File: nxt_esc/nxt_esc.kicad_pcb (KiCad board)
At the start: 2 copper layers, 46.4 x 55.2 mm, 15 parts, among them IC1 L293D, J1 NXT_MOTOR, J2 NXT_MOTOR, SW1 Skid Steer/Drive & Steer, U1 LM7809CT

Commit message: Updated PCB
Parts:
- added C4: 100u, Capacitors_ThroughHole:CP_Radial_D5.0mm_P2.50mm, F.Cu at (154.3, 55.9)
- added C5: 0.1 u, Capacitors_ThroughHole:C_Disc_D3.4mm_W2.1mm_P2.50mm, F.Cu at (158.8, 59.1)
- added C6: 100u, Capacitors_ThroughHole:CP_Radial_D5.0mm_P2.50mm, F.Cu at (153.0, 99.1)
- added C7: 100u, Capacitors_ThroughHole:CP_Radial_D5.0mm_P2.50mm, F.Cu at (160.7, 99.1)
- added C8: 0.1 u, Capacitors_ThroughHole:C_Disc_D3.4mm_W2.1mm_P2.50mm, F.Cu at (159.4, 106.0)
- added C9: 0.1 u, Capacitors_ThroughHole:C_Disc_D3.4mm_W2.1mm_P2.50mm, F.Cu at (153.7, 106.0)
- C3: value 0.1u -> 0.1 u
- U1: value LM7809CT -> LM7805CT
- moved J1 4.44 mm to (171.4, 97.8)
- moved J2 3.81 mm to (141.6, 97.8)
- moved RC1 3.17 mm to (171.4, 57.8)
- moved C2 2.13 mm to (150.0, 88.3), turned to 180 degrees
- moved BT1 1.27 mm to (144.8, 58.4)
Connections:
- BT1 pad 1: Net-(BT1-Pad1) -> VCC
- C3 pad 1: Net-(C2-Pad1) -> GND
- C3 pad 2: GND -> Net-(C2-Pad1)
- U1 pad 1: Net-(BT1-Pad1) -> VCC
- U1 pad 3: VCC -> Net-(C2-Pad1)
- uP1 pad 19: VCC -> Net-(C2-Pad1)
- uP1 pad 22: Net-(C2-Pad1) -> Net-(uP1-Pad22)
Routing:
- net Net-(C2-Pad1): track 121.9 -> 163.5 mm
- net VCC: track 39.9 -> 20.4 mm
- net GND: track 140.1 -> 154.5 mm
- net Net-(C7-Pad2): track 0.00 -> 10.9 mm
- net Net-(C6-Pad2): track 0.00 -> 10.7 mm
- net Net-(IC1-Pad1): track 21.0 -> 31.0 mm
- net Net-(BT1-Pad1): track 9.68 -> 0.00 mm
- net Net-(IC1-Pad15): track 45.6 -> 39.7 mm
- net Net-(J1-Pad6): track 22.3 -> 26.8 mm
- net Net-(J1-Pad5): track 29.3 -> 33.7 mm
- net Net-(IC1-Pad2): track 12.8 -> 16.9 mm
- net Net-(J2-Pad5): track 32.6 -> 36.6 mm
- net Net-(IC1-Pad3): track 40.0 -> 36.3 mm
- net Net-(IC1-Pad14): track 22.0 -> 18.5 mm
- net Net-(IC1-Pad10): track 46.2 -> 49.2 mm
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
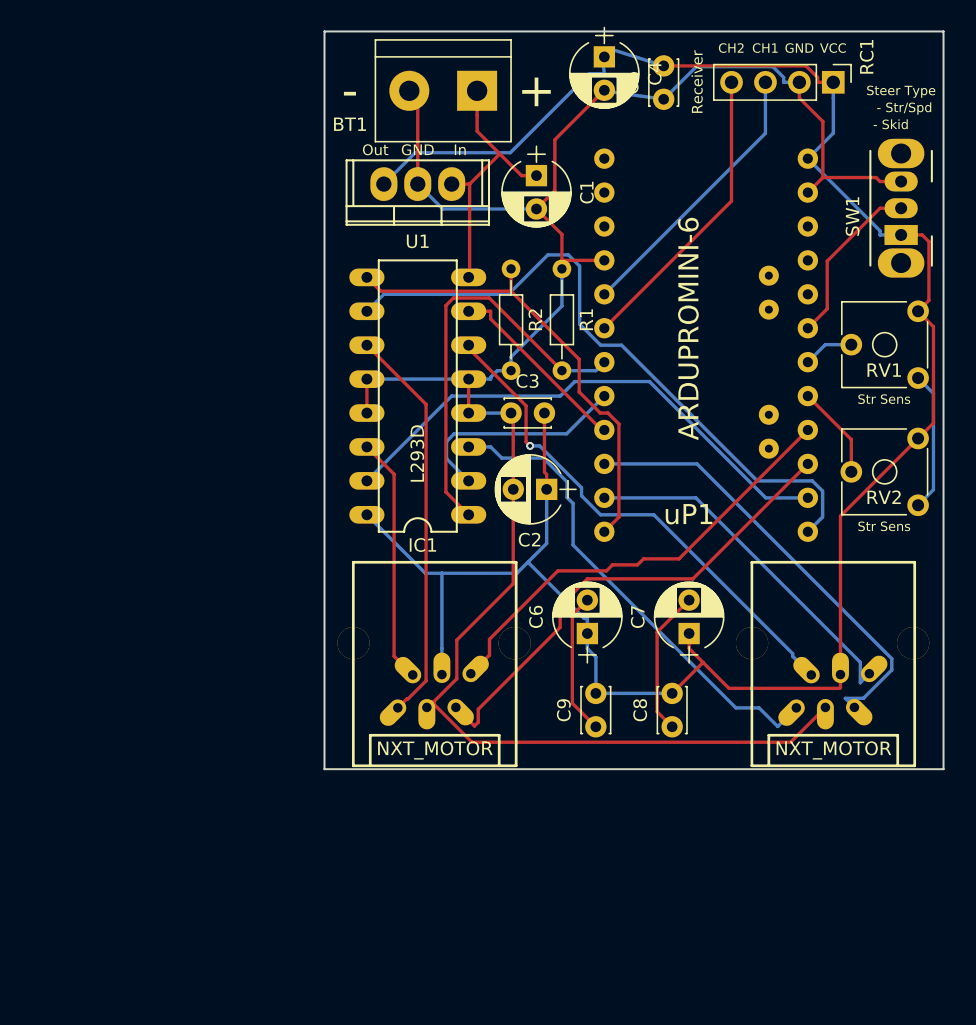
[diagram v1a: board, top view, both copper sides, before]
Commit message: Resized board to 6x6 Lego size
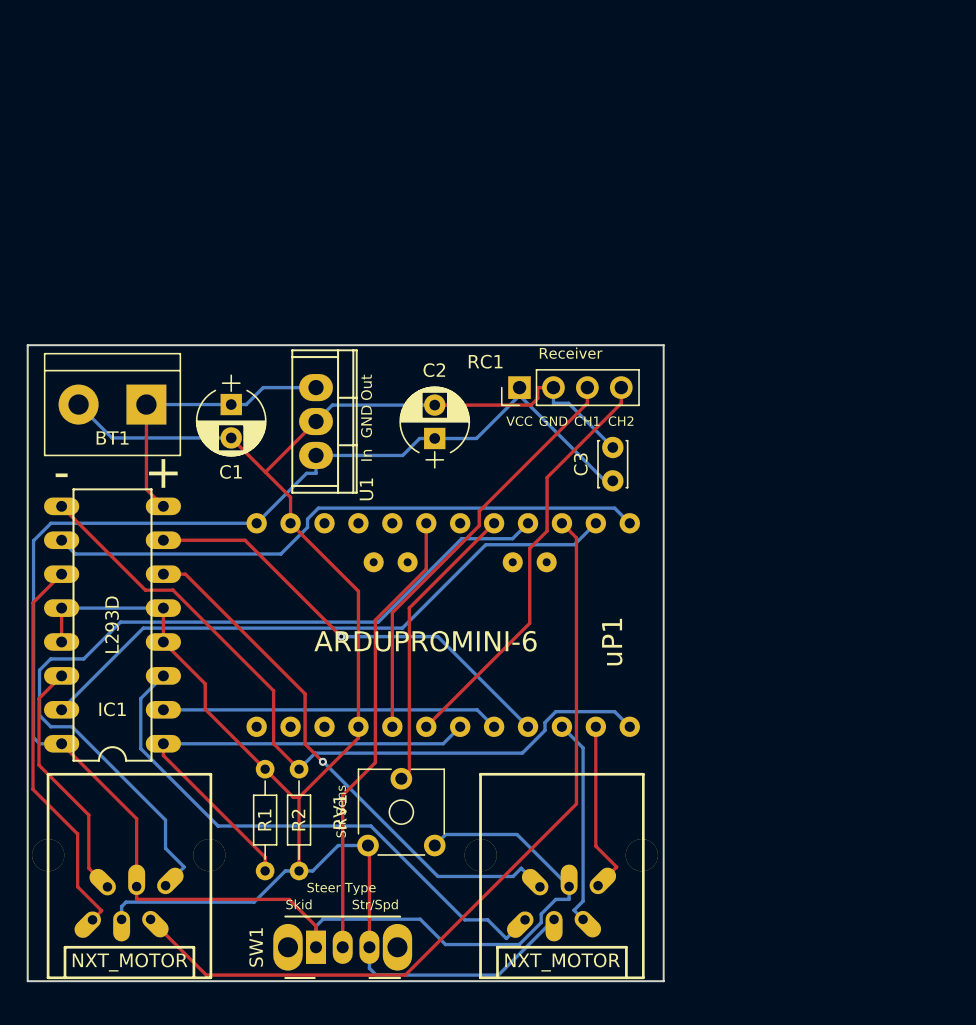
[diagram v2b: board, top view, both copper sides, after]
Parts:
- removed C4, C6, C7: 100u, Capacitors_ThroughHole:CP_Radial_D5.0mm_P2.50mm
- removed C5, C8, C9: 0.1 u, Capacitors_ThroughHole:C_Disc_D3.4mm_W2.1mm_P2.50mm
- removed RV2: Steering Sensitivity, Potentiometers:Potentiometer_Trimmer_ACP_CA6v_Horizontal
- RV1: value Steering Trim -> Steering Sensitivity
- moved SW1 69.0 mm to (132.7, 122.6), turned to 0 degrees
- moved uP1 59.5 mm to (121.9, 108.6), turned to 90 degrees
- moved RV1 53.9 mm to (141.6, 114.9), turned to 90 degrees
- moved R1 43.6 mm to (128.9, 109.2)
- moved R2 40.7 mm to (131.4, 109.2)
- moved BT1 34.1 mm to (120.0, 81.9)
- moved RC1 32.8 mm to (148.0, 80.6), turned to 90 degrees
- moved IC1 28.6 mm to (117.5, 98.4)
- moved C1 28.6 mm to (126.4, 81.9)
- moved J2 27.8 mm to (118.7, 113.7)
- moved J1 25.8 mm to (151.1, 113.7)
- moved U1 19.3 mm to (132.7, 83.2), turned to 270 degrees
- moved C2 9.21 mm to (141.6, 84.5), turned to 90 degrees
- moved C3 9.16 mm to (154.9, 87.6), turned to 90 degrees
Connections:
- C3 pad 1: GND -> Net-(C2-Pad1)
- C3 pad 2: Net-(C2-Pad1) -> GND
- RV1 pad 3: Net-(RV1-Pad3) -> GND
- uP1 pad 25: Net-(RV1-Pad2) -> Net-(uP1-Pad25)
- uP1 pad 26: Net-(RV2-Pad2) -> Net-(RV1-Pad2)
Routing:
- net Net-(J2-Pad6): track 33.5 -> 63.3 mm
- net Net-(C2-Pad1): track 163.5 -> 135.0 mm
- net Net-(J2-Pad5): track 36.6 -> 60.4 mm
- net Net-(SW1-Pad2): track 12.8 -> 34.3 mm
- net Net-(IC1-Pad9): track 35.0 -> 55.6 mm
- net Net-(IC1-Pad7): track 14.2 -> 33.1 mm, vias 0 -> 1
- net Net-(RV1-Pad2): track 3.80 -> 22.0 mm
- net Net-(J1-Pad5): track 33.7 -> 15.6 mm
- net Net-(J1-Pad6): track 26.8 -> 13.1 mm
- net Net-(C7-Pad2): track 10.9 -> 0.00 mm
- net Net-(C6-Pad2): track 10.7 -> 0.00 mm
- net Net-(RC1-Pad3): track 20.9 -> 31.4 mm
- net Net-(RV1-Pad3): track 10.5 -> 0.00 mm
- net Net-(RC1-Pad4): track 22.4 -> 31.4 mm
- net Net-(IC1-Pad2): track 16.9 -> 25.3 mm
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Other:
- board size 46.4 x 55.2 mm -> 47.6 x 47.6 mm
- board text added: "Skid"
- board text added: "Str/Spd"
- board text removed: "- Skid"
- board text removed: "- Str/Spd"

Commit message: Added center steering button
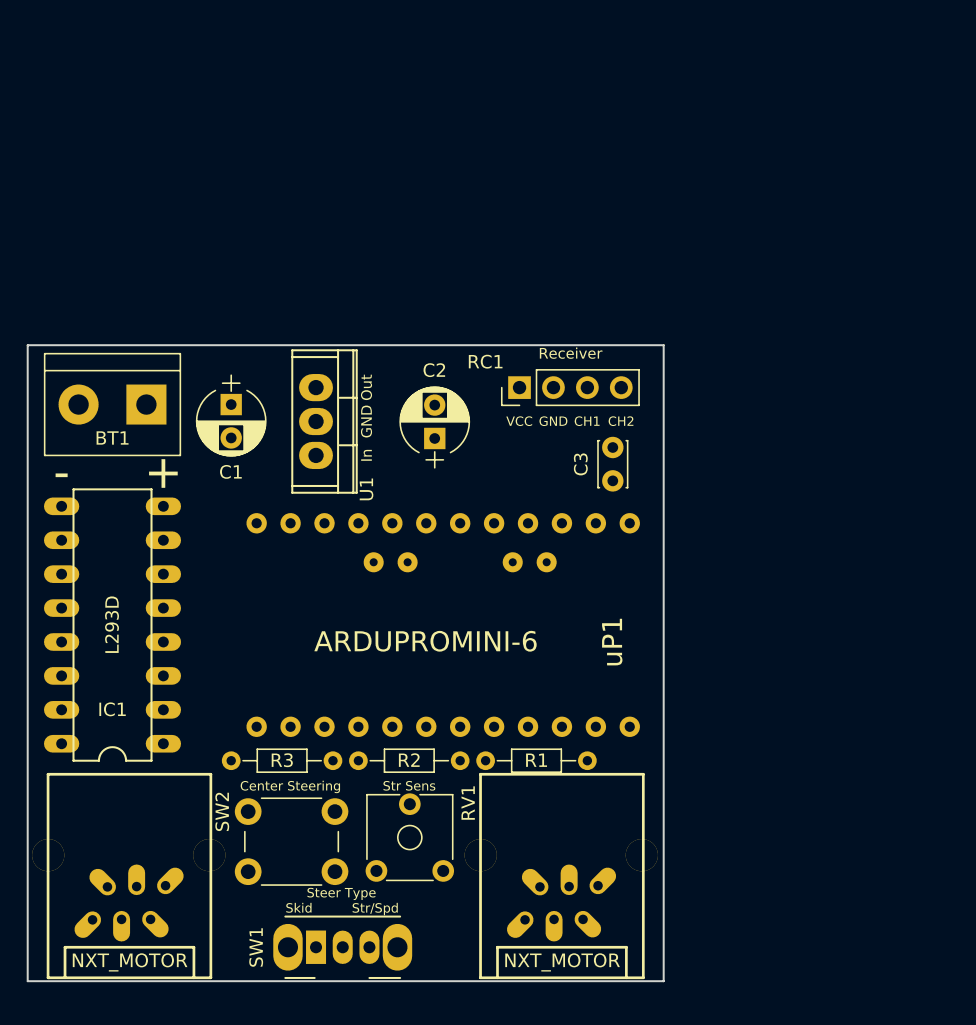
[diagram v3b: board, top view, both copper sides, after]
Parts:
- added R3: 100k, Resistors_ThroughHole:R_Axial_DIN0204_L3.6mm_D1.6mm_P7.62mm_Horizontal, F.Cu at (126.4, 108.6)
- added SW2: Center Steering, Buttons_Switches_ThroughHole:SW_PUSH_6mm, F.Cu at (127.6, 112.4)
- moved R1 16.5 mm to (145.4, 108.6), turned to 0 degrees
- moved R2 12.1 mm to (143.5, 108.6), turned to 180 degrees
- moved RV1 2.01 mm to (142.2, 116.8)
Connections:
- uP1 pad 21: Net-(uP1-Pad21) -> (no net)
- uP1 pad 22: Net-(uP1-Pad22) -> (no net)
- uP1 pad 23: Net-(uP1-Pad23) -> (no net)
- uP1 pad 31: Net-(uP1-Pad31) -> (no net)
- uP1 pad 32: Net-(uP1-Pad32) -> (no net)
- uP1 pad 34: Net-(uP1-Pad34) -> (no net)
- uP1 pad 35: Net-(uP1-Pad35) -> (no net)
- uP1 pad 7: Net-(uP1-Pad7) -> (no net)
- uP1 pad 8: Net-(uP1-Pad8) -> (no net)
- uP1 pad 9: Net-(uP1-Pad9) -> (no net)
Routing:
- net GND: track 157.4 -> 0.00 mm
- net Net-(C2-Pad1): track 135.0 -> 0.00 mm
- net Net-(J2-Pad6): track 63.3 -> 0.00 mm
- net Net-(J2-Pad5): track 60.4 -> 0.00 mm
- net Net-(IC1-Pad9): track 55.6 -> 0.00 mm
- net Net-(IC1-Pad15): track 45.8 -> 0.00 mm
- net Net-(IC1-Pad10): track 45.2 -> 0.00 mm
- net Net-(IC1-Pad3): track 41.4 -> 0.00 mm
- net Net-(IC1-Pad6): track 40.6 -> 0.00 mm, vias 1 -> 0
- net Net-(IC1-Pad1): track 35.4 -> 0.00 mm
- net Net-(SW1-Pad2): track 34.3 -> 0.00 mm
- net Net-(IC1-Pad7): track 33.1 -> 0.00 mm, vias 1 -> 0
- net Net-(RC1-Pad4): track 31.4 -> 0.00 mm
- net Net-(RC1-Pad3): track 31.4 -> 0.00 mm
- net Net-(IC1-Pad11): track 29.2 -> 0.00 mm
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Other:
- board text added: "Center Steering"

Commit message: Added motor jack labels. Forgot to route wires.
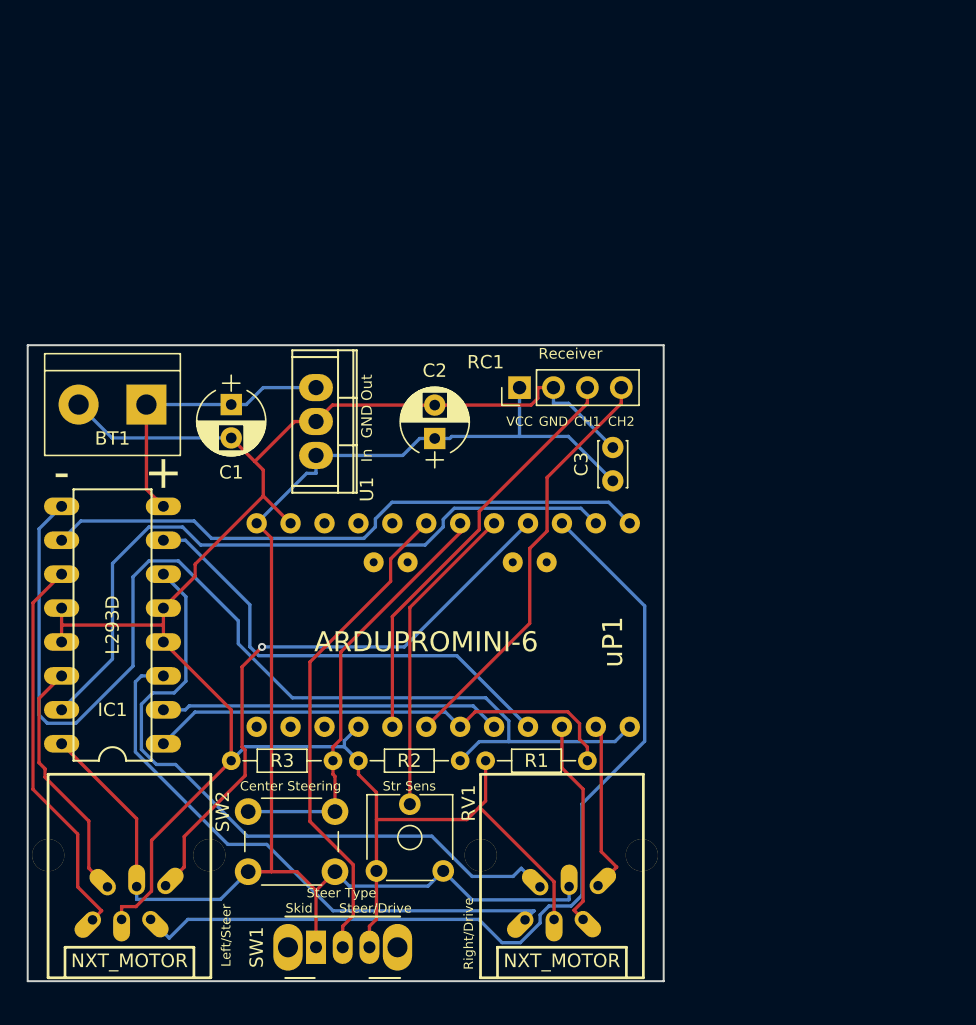
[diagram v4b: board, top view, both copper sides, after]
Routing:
- net GND: track 0.00 -> 153.5 mm
- net Net-(C2-Pad1): track 0.00 -> 117.2 mm
- net Net-(IC1-Pad9): track 0.00 -> 82.0 mm
- net Net-(J2-Pad5): track 0.00 -> 68.4 mm
- net Net-(IC1-Pad15): track 0.00 -> 52.4 mm
- net Net-(IC1-Pad6): track 0.00 -> 50.8 mm
- net Net-(IC1-Pad10): track 0.00 -> 45.8 mm
- net Net-(J2-Pad6): track 0.00 -> 44.8 mm, vias 0 -> 1
- net Net-(IC1-Pad3): track 0.00 -> 43.3 mm
- net Net-(SW1-Pad2): track 0.00 -> 37.0 mm
- net Net-(IC1-Pad1): track 0.00 -> 36.5 mm
- net Net-(IC1-Pad7): track 0.00 -> 34.9 mm
- net Net-(R3-Pad2): track 0.00 -> 32.1 mm
- net Net-(RC1-Pad4): track 0.00 -> 31.4 mm
- net Net-(RC1-Pad3): track 0.00 -> 31.4 mm
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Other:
- board text added: "Left/Steer"
- board text added: "Right/Drive"
- board text added: "Steer/Drive"
- board text removed: "Str/Spd"

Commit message: Added reverse polarity protection diode and power switch
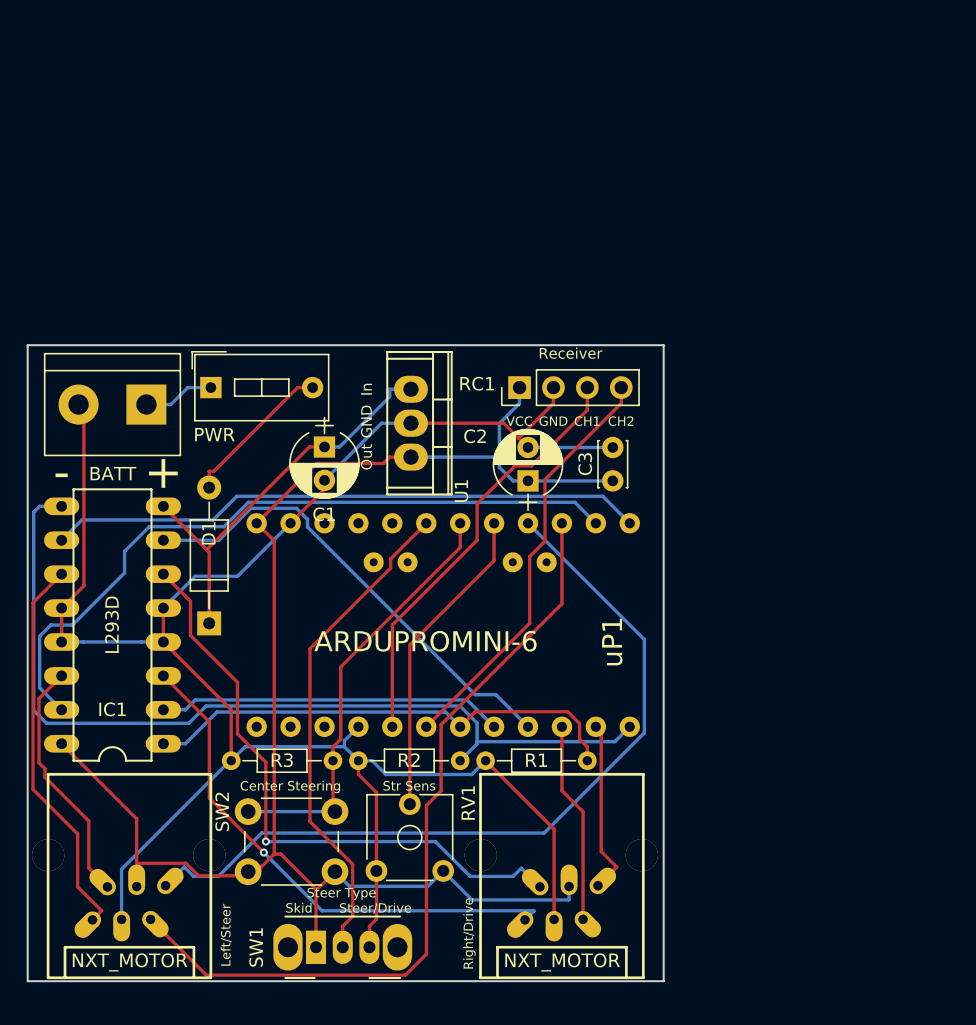
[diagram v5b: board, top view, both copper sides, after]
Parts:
- added D1: D_Schottky, Diodes_ThroughHole:D_A-405_P10.16mm_Horizontal, F.Cu at (124.7, 98.3)
- added PWR: SPST, Buttons_Switches_ThroughHole:SW_DIP_x1_W7.62mm_Slide, F.Cu at (124.8, 80.6)
- moved C2 7.67 mm to (148.6, 87.6)
- moved C1 7.67 mm to (133.3, 85.1)
- moved U1 7.11 mm to (139.8, 83.3)
- renumbered BT1 to BATT
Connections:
- BATT pad 1: VCC -> Net-(BT1-Pad1)
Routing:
- net Net-(J2-Pad6): track 44.8 -> 60.5 mm, vias 1 -> 0
- net Net-(IC1-Pad9): track 82.0 -> 67.0 mm
- net Net-(D1-Pad2): track 0.00 -> 11.6 mm
- net VCC: track 21.4 -> 30.8 mm
- net Net-(J2-Pad5): track 68.4 -> 59.5 mm
- net Net-(BT1-Pad1): track 0.00 -> 5.35 mm
- net Net-(IC1-Pad6): track 50.8 -> 45.6 mm, vias 0 -> 1
- net Net-(IC1-Pad3): track 43.3 -> 39.3 mm, vias 0 -> 1
- net GND: track 153.5 -> 152.0 mm
- net Net-(IC1-Pad15): track 52.4 -> 53.6 mm
- net Net-(IC1-Pad10): track 45.8 -> 44.7 mm
- net Net-(C2-Pad1): track 117.2 -> 116.3 mm
- net Net-(RC1-Pad3): track 31.4 -> 32.2 mm
- net Net-(J1-Pad5): track 15.6 -> 15.1 mm

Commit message: Updated components to ones I already have
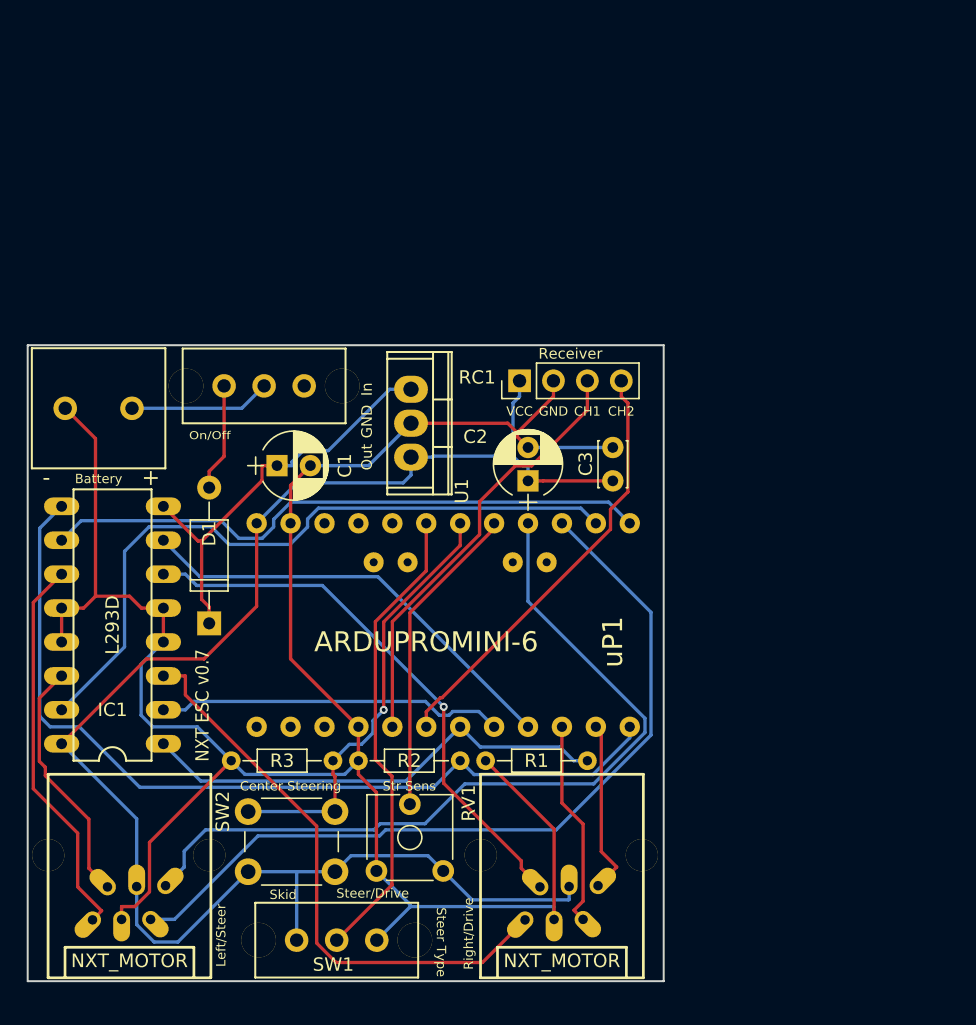
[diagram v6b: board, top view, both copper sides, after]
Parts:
- removed BATT: Battery, Terminal_Blocks:TerminalBlock_bornier-2_P5.08mm
- removed PWR: SPST, Buttons_Switches_ThroughHole:SW_DIP_x1_W7.62mm_Slide
- added Battery: Battery, nxt_sec_lib:SCREW_TERMINAL_JRL, F.Cu at (116.4, 82.2)
- added On/Off: Power, nxt_sec_lib:SLIDE_SWITCH_JRL, F.Cu at (128.8, 80.5)
- SW1: footprint Buttons_Switches_ThroughHole:SW_CuK_OS102011MA1QN1_SPDT_Angled -> nxt_sec_lib:SLIDE_SWITCH_JRL
- moved C1 3.82 mm to (129.8, 86.5), turned to 0 degrees
- moved SW1 1.64 mm to (134.3, 122.0)
- moved RC1 0.51 mm to (148.0, 80.1)
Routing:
- net GND: track 152.0 -> 165.6 mm
- net Net-(BT1-Pad1): track 5.35 -> 10.6 mm
- net Net-(C2-Pad1): track 116.3 -> 120.8 mm
- net Net-(IC1-Pad6): track 45.6 -> 41.6 mm
- net Net-(IC1-Pad3): track 39.3 -> 43.3 mm, vias 1 -> 0
- net Net-(D1-Pad2): track 11.6 -> 8.08 mm
- net Net-(IC1-Pad7): track 35.4 -> 33.1 mm
- net Net-(J2-Pad5): track 59.5 -> 61.8 mm
- net Net-(SW1-Pad2): track 37.0 -> 35.0 mm
- net Net-(IC1-Pad15): track 53.6 -> 52.4 mm
- net Net-(IC1-Pad10): track 44.7 -> 45.8 mm
- net Net-(IC1-Pad9): track 67.0 -> 66.0 mm
- net Net-(RC1-Pad4): track 31.4 -> 32.4 mm
- net Net-(IC1-Pad1): track 36.5 -> 35.6 mm
- net VCC: track 30.8 -> 31.5 mm
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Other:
- board text added: "NXT ESC v0.7"
